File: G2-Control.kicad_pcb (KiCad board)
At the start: 2 copper layers, 100 x 100 mm, 92 parts, among them J1 Conn_01x06_Pin, J102 Conn_01x06_Pin, J103 Conn_01x06_Pin, J104 Board Interconnect, J2 Q2_link, J3 Conn_01x07_Pin, J4 Conn_01x05_Pin, K1 SMI-12VDC-SL-2C, K2 SMI-12VDC-SL-2C, K3 SMI-12VDC-SL-2C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

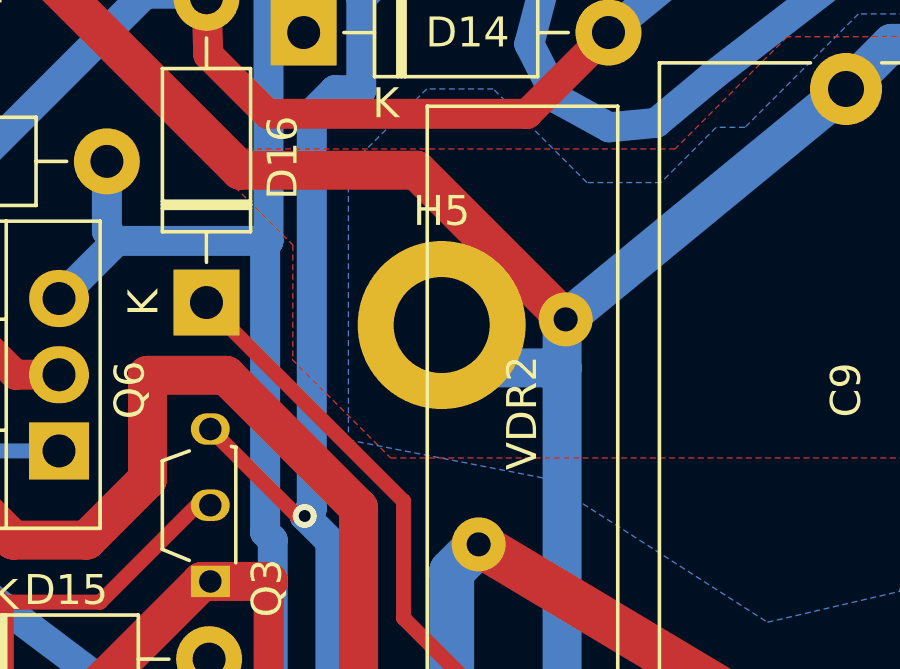
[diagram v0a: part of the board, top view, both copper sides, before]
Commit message: Update component properties and positioning in PCB layout
Several updates were made to the properties and positions of various components in the PCB layout file due to changes in the schematic.
The Value property for numerous elements was changed, appending an asterisk at the end.
Additionally, the Reference positions, Datasheet, and Description fields were modified for certain components.
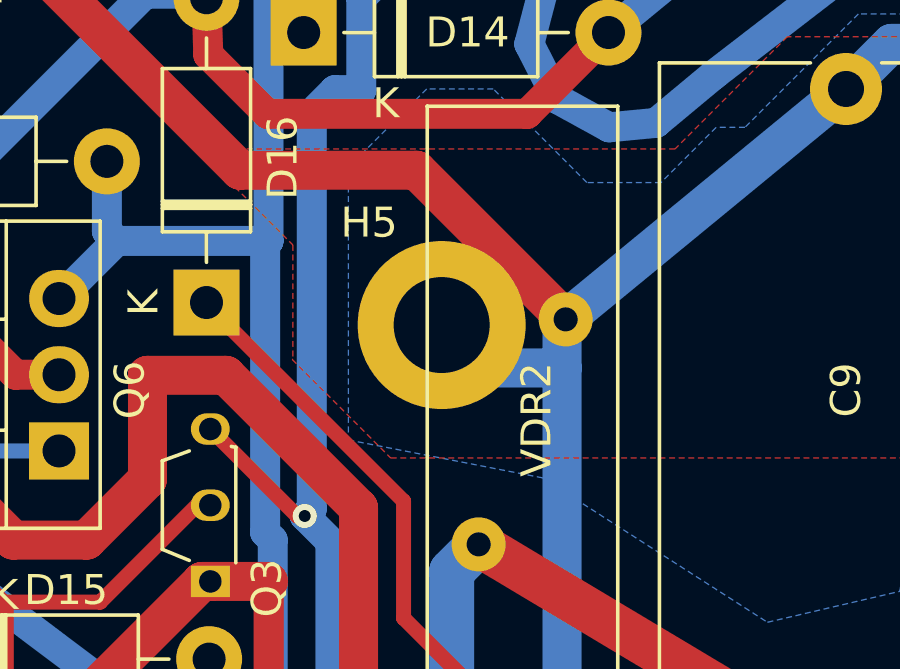
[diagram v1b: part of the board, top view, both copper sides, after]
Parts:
- R10: value 150k 1W [150k 1W] -> 150k 1W*
- R13: value 10k 2W typ -> 10k 2W*
- R15: value 82R 1W [82R 1W] -> 82R 1W*
- VDR2: value V320LA40B [V320LA40B] -> V320LA40B*
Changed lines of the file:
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@@
 			)
 		)
-		(property "Value" "150k 1W [150k 1W]"
+		(property "Value" "150k 1W*"
 			(at 2.54 3.37 90)
 			(layer "F.Fab")
@@
 		(tags "varistor SIOV")
 		(property "Reference" "VDR2"
-			(at 4.385 1.45 90)
+			(at 4.161069 1.926787 90)
 			(layer "F.SilkS")
 			(effects
@@
 			)
 		)
-		(property "Value" "V320LA40B [V320LA40B]"
+		(property "Value" "V320LA40B*"
 			(at 3.75 -2.6 90)
 			(layer "F.Fab")
@@
 			)
 		)
-		(property "Value" "82R 1W [82R 1W]"
+		(property "Value" "82R 1W*"
 			(at 2.54 3.37 0)
 			(layer "F.Fab")
@@
 			)
 		)
-		(property "Value" "10k 2W typ"
+		(property "Value" "10k 2W*"
 			(at 2.54 3.37 90)
 			(layer "F.Fab")
@@
 			)
 		)
-		(property "Datasheet" "https://www.electrokit.com/uploads/productfile/41017/2N5060-D.pdf"
+		(property "Datasheet" ""
 			(at 0 0 90)
 			(unlocked yes)
@@
 			)
 		)
-		(property "Description" ""
+		(property "Description" "Silicon controlled rectifier, cathode/gate/anode"
 			(at 0 0 90)
 			(unlocked yes)
@@
 		(tags "mounting hole 3.2mm m3 din965")
 		(property "Reference" "H5"
-			(at 0 -3.8 0)
+			(at -2.42 -3.41 0)
 			(layer "F.SilkS")
 			(effects
@@
 			(pts
 				(xy 125.16 67.33) (xy 131.63 68.592813) (xy 139.128815 73.407282) (xy 143.539755 72.376829) (xy 145.915928 58.889776)
-				(xy 160.92 58.976194) (xy 158.73 53.005619) (xy 146.944236 53.14) (xy 146.93 53.13) (xy 146.93 53.13)
-				(xy 146.93 53.13) (xy 142.16 53.13) (xy 138.38 56.91) (xy 137.42 56.91) (xy 135.58 58.75) (xy 133.11 58.75)
-				(xy 129.99 55.63) (xy 127.77 55.63) (xy 125.16 58.24)
+				(xy 160.92 58.976194) (xy 158.73 53.005619) (xy 146.944236 53.14) (xy 146.93 53.13) (xy 142.16 53.13)
+				(xy 138.38 56.91) (xy 137.42 56.91) (xy 135.58 58.75) (xy 133.11 58.75) (xy 129.99 55.63) (xy 127.77 55.63)
+				(xy 125.16 58.24)
 			)
 		)

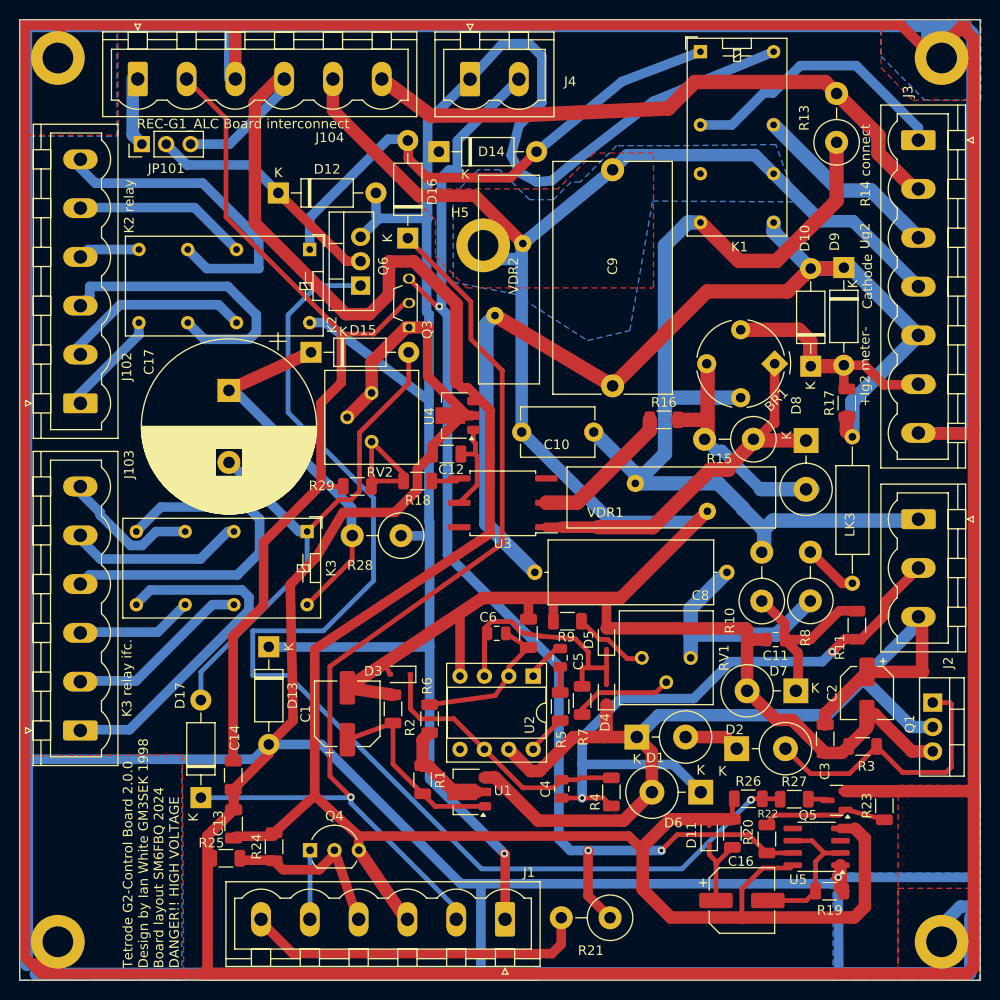
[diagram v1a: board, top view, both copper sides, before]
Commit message: Replaced Q4 transistor schematic symbol BC557 with 2N3904 in G2-Control schematic
Updated the G2-Control schematic by replacing the schematic symbol BC557 for transistor Q4 with the symbol for 2N3904 which has the same pin numbering as the actual transistor used. This change fixes
issue #11 and makes the silkscreen print on the PCB show the transistor the way it has to be rotated in order to function properly.

Other changes is that the references and values of the components have been moved and the valye is set in a smaller font to increase readability. The global labels has also been replaced by hierarchical labels.
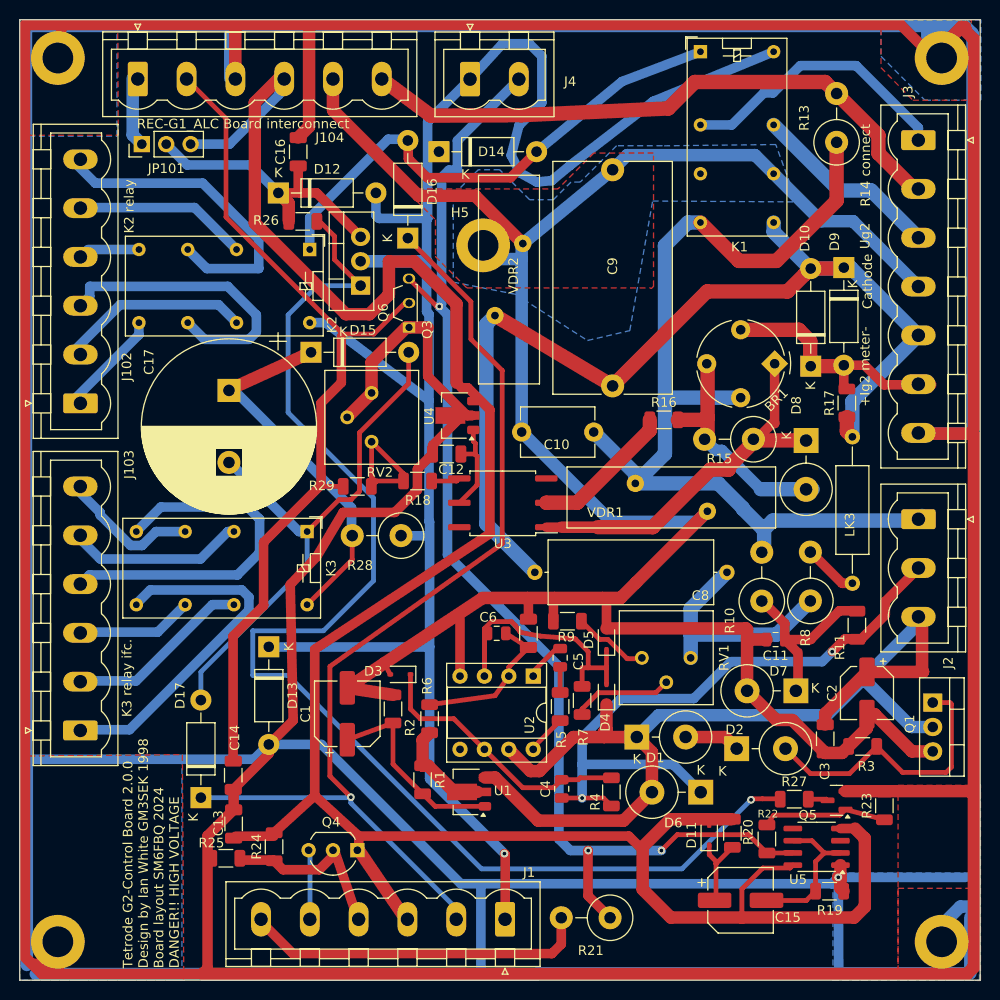
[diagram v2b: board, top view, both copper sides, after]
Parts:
- added C15: 100u 16V, Capacitor_SMD:CP_Elec_6.3x5.7, F.Cu at (155.1, 131.7)
- C16: value 100u 16V -> 100n; footprint Capacitor_SMD:CP_Elec_6.3x5.7 -> Capacitor_SMD:C_1206_3216Metric
- C17: value 2200u 50V -> 330u 25V*
- R15: value 82R 1W* -> 120R 1W*
- R16: value 1k5 -> 820R*
- R20: value 100k -> 100k*
- R28: value 82 2W -> 820 1W*
- R9: value 27k [27k] -> 27k*
- U1: value LM317L_SOT-89 -> LM317L_SOT89
- U2: value 748 -> uA748
- VDR1: value V320LA40B -> V320LA40B*
- moved C16 90.6 mm to (109.0, 53.8), turned to 90 degrees
- moved R26 75.9 mm to (109.5, 61.0)
- moved Q4 4.93 mm to (115.2, 126.5), turned to 180 degrees
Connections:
- net +24V Unreg in renamed /24V Unreg
- net +Ig2 renamed /+Ig2
- net -Ig2 renamed /-Ig2
- net ALARM_LED_CATHODE renamed /Alarm LED -
- net Aux trip in renamed /Aux trip
- net CATHODE renamed /CATHODE
- net G1 trip in renamed /G1 trip
- net G2 UNREG IN renamed /G2 Unreg
- net G2 UNREG TX IN renamed /G2 UNREG TX
- net G2-REG-OUT renamed /G2 reg
- net PTT_L renamed /PTT_L
- net RESET-A renamed /Reset -
- C13 pad 1: +12V REG IN -> +12V
- C16 pad 1: Net-(D11-K) -> Net-(D12-K)
- C16 pad 2: Net-(U5-THR) -> GNDPWR
- D11 pad 2: +12V REG IN -> +12V
- D12 pad 2: +12/24V HV ENABLE -> /HV Enable
- D13 pad 1: +12/24V HV ENABLE -> /HV Enable
- D14 pad 1: +12/24V HV ENABLE -> /HV Enable
- J1 pad 1: +12/24V HV ENABLE -> /HV Enable
- J1 pad 3: +12V REG IN -> +12V
- J1 pad 5: ALARM_LED_ANODE -> /Alarm LED +
- J104 pad 4: +12V REG IN -> +12V
- J4 pad 1: +12/24V HV ENABLE -> /HV Enable
- JP101 pad 3: +12V REG IN -> +12V
- K1 pad 16: +12/24V HV ENABLE -> /HV Enable
- K2 pad 16: +12/24V HV ENABLE -> /HV Enable
- Q4 pad 1: ALARM_LED_ANODE -> +12V
- Q4 pad 3: +12V REG IN -> /Alarm LED +
- Q6 pad 2: Net-(D12-K) -> /HV Enable
- Q6 pad 3: +12/24V HV ENABLE -> Net-(D12-K)
- R20 pad 2: +12V REG IN -> +12V
- R24 pad 2: +12V REG IN -> +12V
- R26 pad 1: +12V REG IN -> Net-(D12-K)
- R28 pad 1: +12/24V HV ENABLE -> /HV Enable
- U4 pad 3: +12V REG IN -> +12V
- U5 pad 4: +12V REG IN -> +12V
- U5 pad 8: +12V REG IN -> +12V
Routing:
- net +12V REG IN: track 240.8 -> 0.00 mm
- net +12V: track 0.00 -> 238.9 mm
- net /HV Enable: track 0.00 -> 195.9 mm, vias 0 -> 1
- net +12/24V HV ENABLE: track 191.7 -> 0.00 mm, vias 1 -> 0
- net GNDPWR: track 1015.8 -> 1027.9 mm
- net Net-(Q6-G): track 125.8 -> 134.5 mm
- net ALARM_LED_ANODE: track 7.48 -> 0.00 mm
- net /Alarm LED +: track 0.00 -> 7.48 mm
- net Net-(D12-K): track 25.3 -> 30.6 mm

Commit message: Updated PCB layout to accommodate new relay model and reworked wiring
Swapped existing Relay model with the Schrack-RT2 model, and updated PCB layout to accommodate the new output routes. Additionally, repositioned the Resistor R13 to ensure optimal grounding. This change aims at achieving lower impedance for the VDR2 and K1 connections to the cathode.
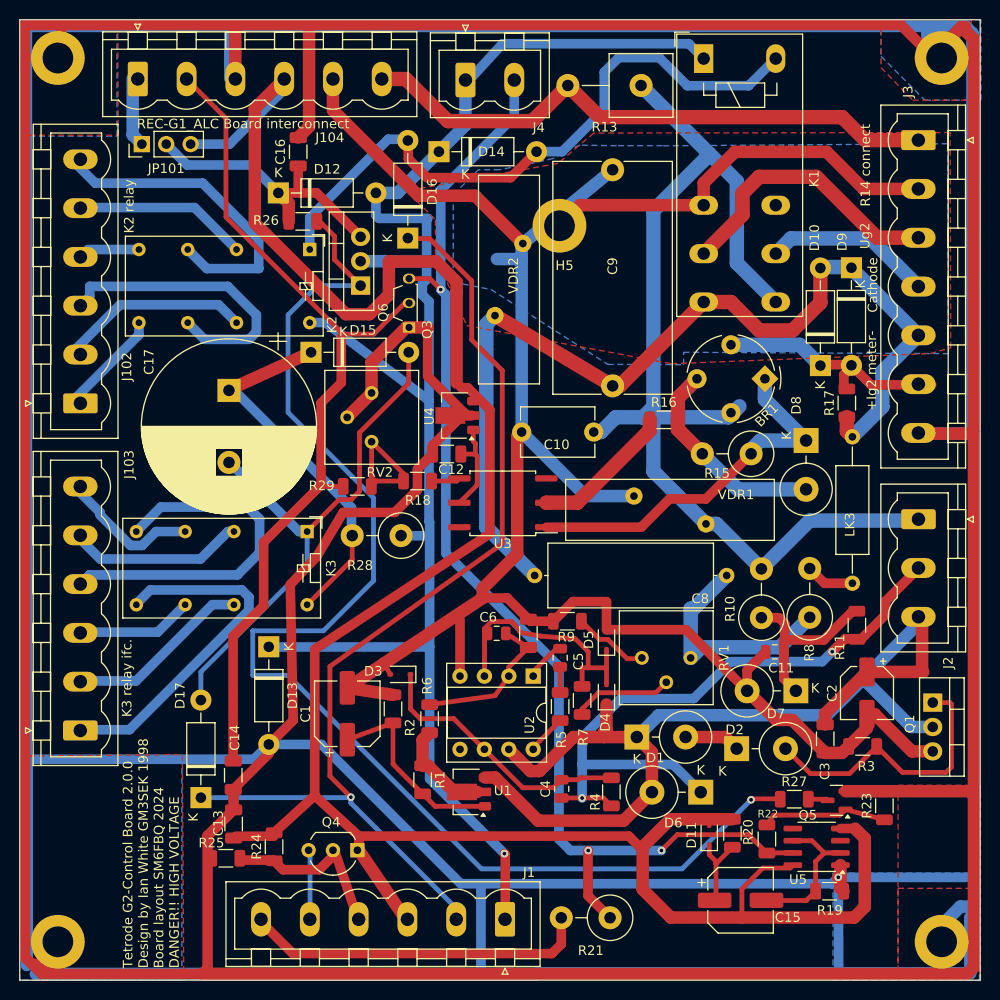
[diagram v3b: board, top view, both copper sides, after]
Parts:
- K1: value SMI-12VDC-SL-2C -> AZ822-2C-24DSE; footprint Relay_THT:Relay_DPDT_Omron_G5V-2 -> Relay_THT:Relay_DPDT_Schrack-RT2-FormC_RM5mm
- K2, K3: value SMI-12VDC-SL-2C -> AZ822-2C-24DSE
- R13: footprint Resistor_THT:R_Axial_DIN0414_L11.9mm_D4.5mm_P5.08mm_Vertical -> Resistor_THT:R_Axial_Power_L20.0mm_W6.4mm_P7.62mm_Vertical
- moved R13 21.2 mm to (144.7, 46.9), turned to 180 degrees
- moved VDR1 8.48 mm to (151.5, 92.5), turned to 180 degrees
- moved H5 8.21 mm to (136.2, 61.5)
- moved BR1 1.87 mm to (157.6, 77.4)
- moved R10 1.73 mm to (157.2, 102.3)
- moved R8 1.71 mm to (162.3, 102.2)
- moved R15 1.53 mm to (156.2, 85.2)
- moved C11 1.28 mm to (158.6, 105.8)
- moved D10 1.01 mm to (163.4, 76.0)
- moved K1 0.79 mm to (151.2, 44.1), turned to -90 degrees
- moved D9 0.79 mm to (166.6, 65.8)
- moved J4 0.49 mm to (126.4, 46.3)
- moved C8 0.33 mm to (153.6, 97.9)
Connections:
- J3 pad 1: /G2 UNREG TX -> /G2 Unreg
- J3 pad 2: /G2 Unreg -> /CATHODE
- J3 pad 4: /CATHODE -> /G2 UNREG TX
- K1 pad 11: /CATHODE -> /G2 reg
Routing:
- net /HV Enable: track 195.9 -> 169.8 mm
- net Net-(D14-A): track 54.3 -> 67.7 mm
- net /G2 UNREG TX: track 29.2 -> 17.6 mm
- net /R12: track 105.3 -> 115.6 mm
- net /G2 reg: track 19.9 -> 29.6 mm
- net /CATHODE: track 240.3 -> 234.8 mm
- net /-Ig2: track 108.6 -> 103.6 mm
- net Net-(BR1--): track 24.4 -> 22.0 mm
- net /G2 Unreg: track 63.5 -> 61.6 mm
- net Net-(BR1-+): track 39.9 -> 38.5 mm
- net Net-(J102-Pin_4): track 6.41 -> 5.32 mm
- net +12V: track 238.9 -> 239.9 mm
- net /Aux trip: track 125.9 -> 125.1 mm
- net Net-(D7-K): track 19.2 -> 18.6 mm

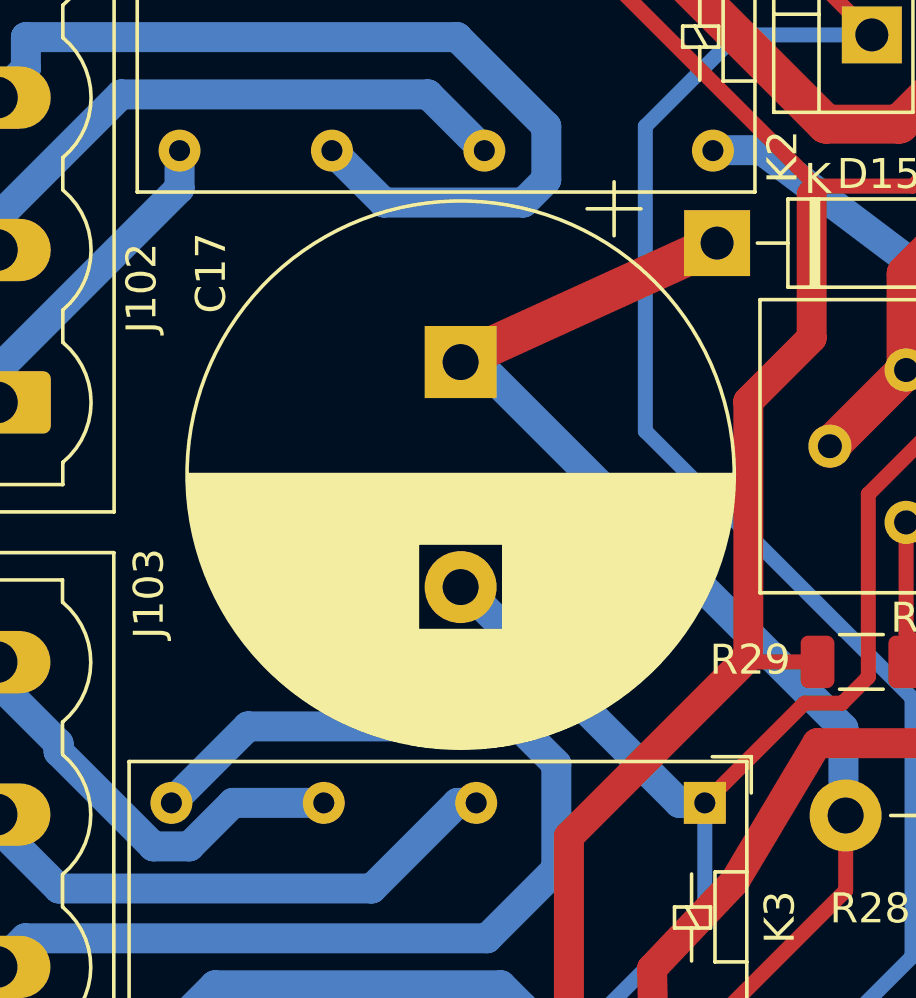
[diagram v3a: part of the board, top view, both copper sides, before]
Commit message: Updated capacitor C17. With the smaller relay and higher voltage, coil current is much less so 100 uF gives some 300-500 mS delay.
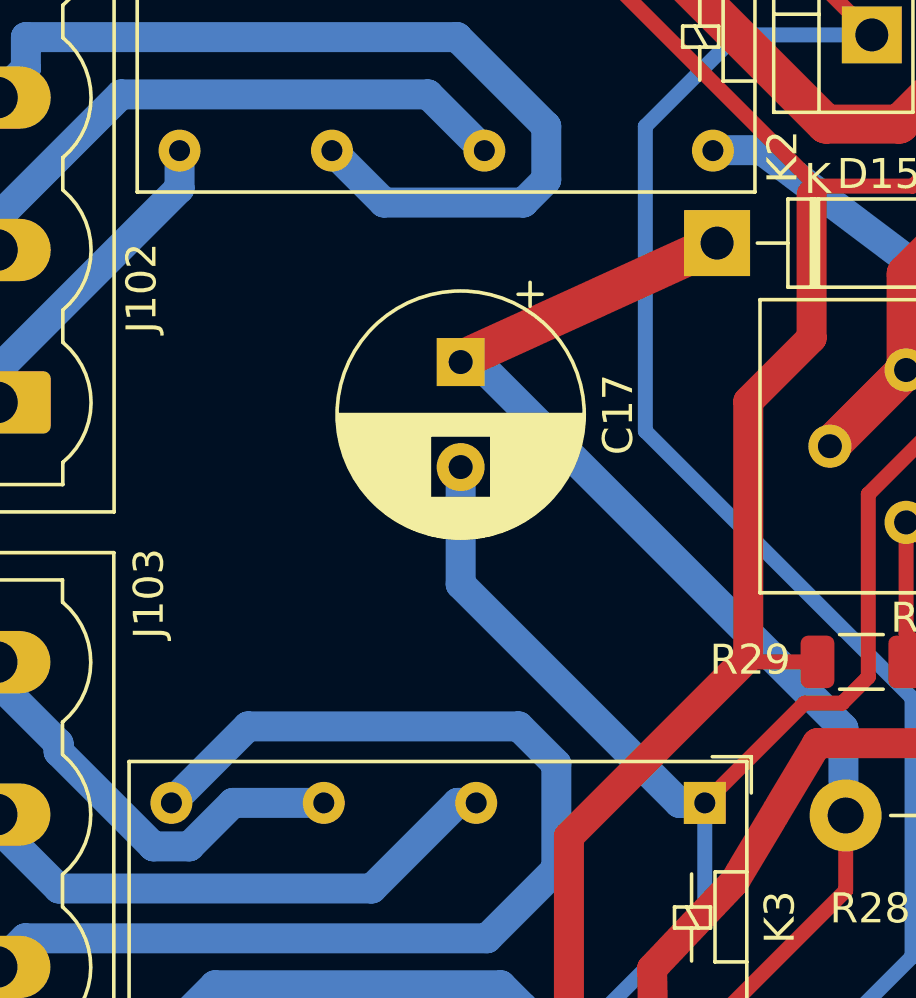
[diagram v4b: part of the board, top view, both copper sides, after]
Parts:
- C17: value 330u 25V* -> 100u 50V*; footprint Capacitor_THT:CP_Radial_D18.0mm_P7.50mm -> Capacitor_THT:CP_Radial_D8.0mm_P3.50mm
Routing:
- net Net-(D15-A): track 57.0 -> 61.0 mm
